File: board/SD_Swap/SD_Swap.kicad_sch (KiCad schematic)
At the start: 45 parts, among them J1 USB_C, Q1 Q_Dual_PNP_PNP_E1B1C2E2B2C1, U1 74LVC2G14, U2 RTS5306E, U3 PCB_SD, U4 93AAxxAT, U5 TS3A27518ERTW, U6 SD_SOCKET, U7 AZ1117-3.3, Y1 12MHz

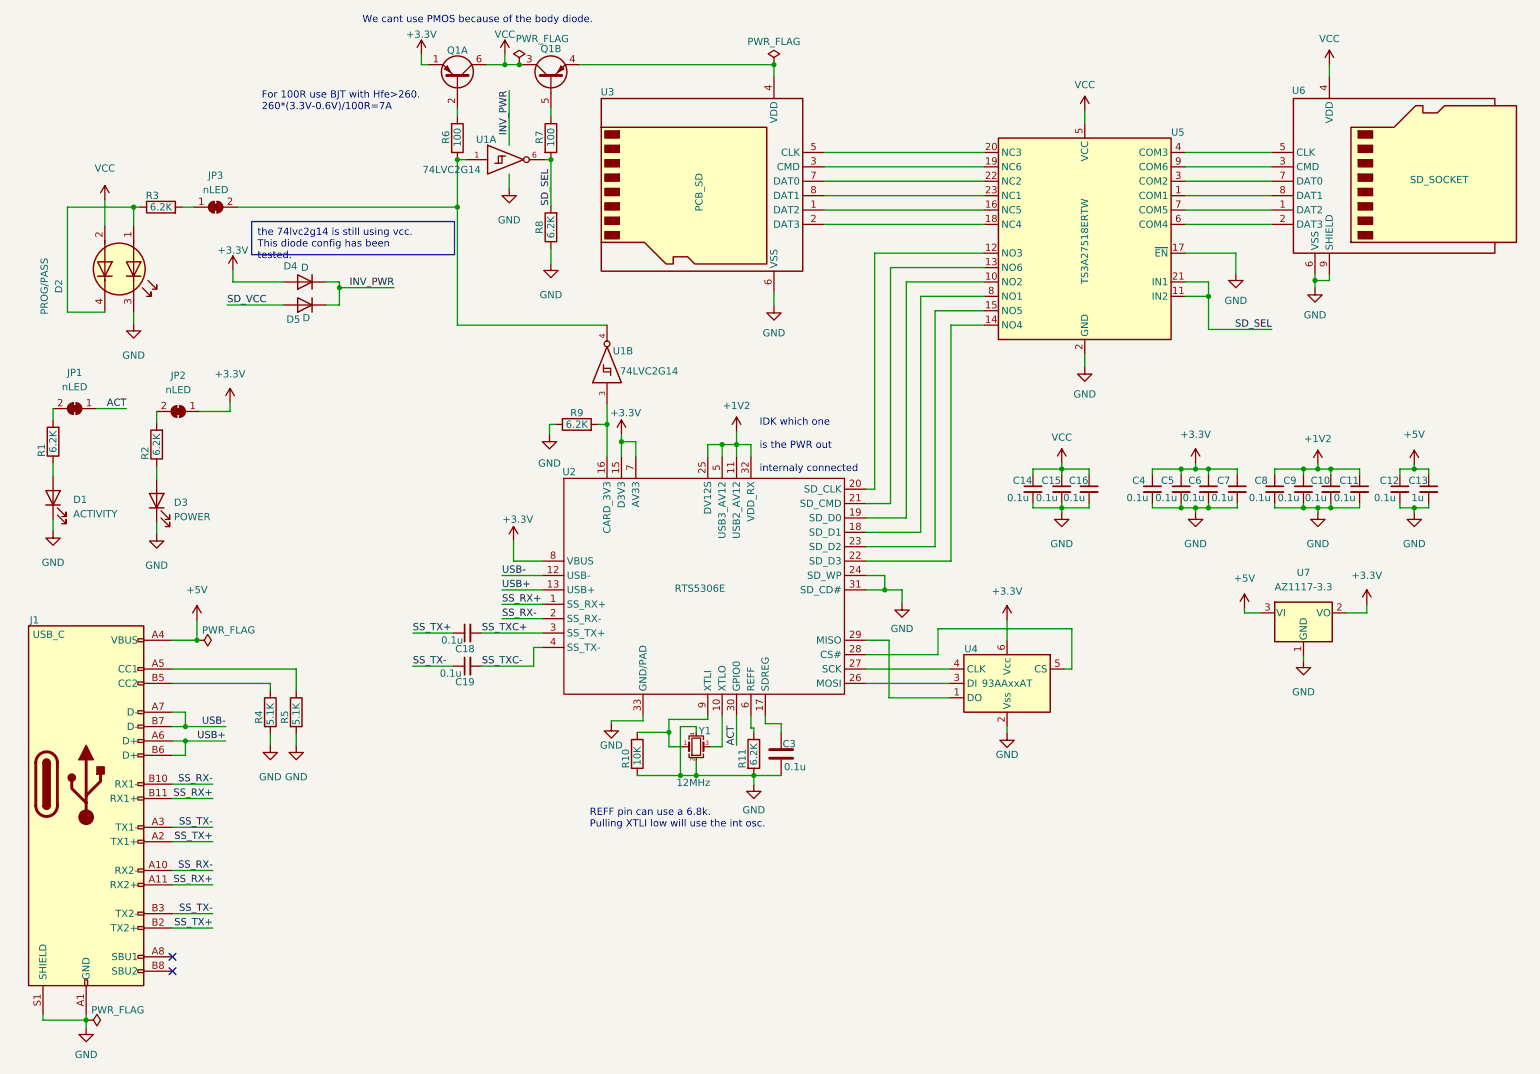
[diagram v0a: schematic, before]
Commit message: update PCB to fix USB3 issues
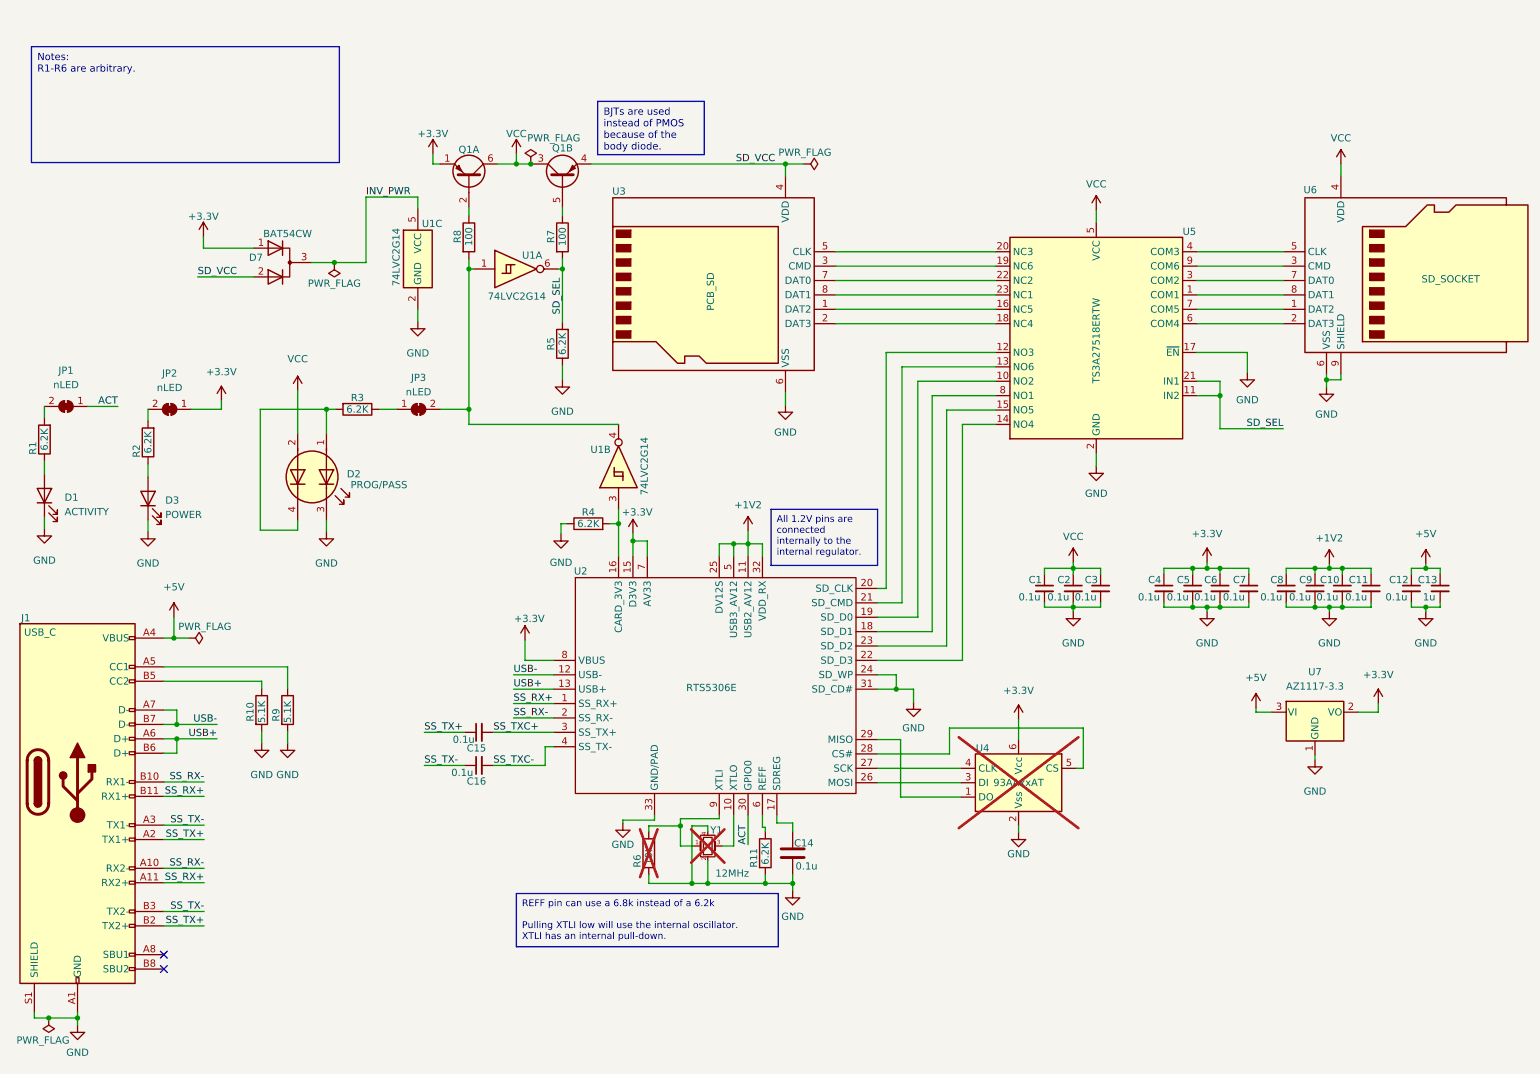
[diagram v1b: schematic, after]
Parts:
- removed D4, D5: D, Diode_SMD:D_0201_0603Metric, symbol Device:D
- added D7: BAT54CW, Package_TO_SOT_SMD:SOT-323_SC-70, symbol Device:D_Dual_CommonCathode_AAK_Parallel
- added unit 3 of U1
- JP1, JP2, JP3, U3: now left out of the parts list
- R6: renamed from R10; now not fitted; now left out of the parts list
- U1: footprint Package_TO_SOT_SMD:SOT-23-6 -> Package_TO_SOT_SMD:SOT-363_SC-70-6; LCSC C12401 -> C3294721
- U4, Y1: now not fitted; now left out of the parts list
- renumbered C14 to C1, C3 to C14, C18 to C15, C19 to C16, C15 to C2, C16 to C3, R4 to R10, R9 to R4, R8 to R5, R6 to R8, R5 to R9
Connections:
- net +3.3V: now also D7.1 (K)
- net GND: now also U1.2 (GND); no longer U1.2 (GND), U1.2 (GND)
- net SD_VCC: now also Q1.4 (E2), U3.4 (VDD), D7.2 (K)
- net VCC: no longer U1.5 (VCC), U1.5 (VCC)
- net at JP3.1 (A): now also R3.1; no longer R3.2
- net at D2.1 (A1), D2.4 (K2): now also R3.2; no longer R3.1
- new net INV_PWR: D7.3 (A), U1.5 (VCC)
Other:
- note removed: "For 100R use BJT with Hfe>260. 260*(3.3V-0.6V)/100R=7A"
- note removed: "IDK which one is the PWR out internaly connected"
- note removed: "REFF pin can use a 6.8k. Pulling XTLI low will use the int osc."
- note removed: "We cant use PMOS because of the body diode."
- title: (none) -> SD SWAP
- moved on the sheet: C1, C10, C11, C12, C13, C14, C15, C16, C2, C3, C4, C5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

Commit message: tmp
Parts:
- J1: footprint Connector_USB:USB_C_Receptacle_Amphenol_12401548E4-2A -> USB-C:USB_C_Receptacle_Amphenol_10137061-00021LF; LCSC C3197851 -> C3197967; Part Number 12401548E4 -> 10137061-00021LF
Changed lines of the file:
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@@
       (effects (font (size 1.27 1.27)))
     )
-    (property "Footprint" "Connector_USB:USB_C_Receptacle_Amphenol_12401548E4-2A" (at 29.972 147.701 0)
+    (property "Footprint" "USB-C:USB_C_Receptacle_Amphenol_10137061-00021LF" (at 29.972 147.701 0)
       (effects (font (size 1.27 1.27)) hide)
     )
-    (property "Datasheet" "https://www.usb.org/sites/default/files/documents/usb_type-c.zip" (at 29.972 147.701 0)
+    (property "Datasheet" "https://www.amphenol-cs.com/media/wysiwyg/files/drawing/10137061.pdf" (at 29.972 147.701 0)
       (effects (font (size 1.27 1.27)) hide)
     )
-    (property "LCSC" "C3197851" (at 26.162 147.701 0)
+    (property "LCSC" "C3197967" (at 26.162 147.701 0)
       (effects (font (size 1.27 1.27)) hide)
     )
-    (property "Part Number" "12401548E4" (at 26.162 147.701 0)
+    (property "Part Number" "10137061-00021LF" (at 26.162 147.701 0)
       (effects (font (size 1.27 1.27)) hide)
     )

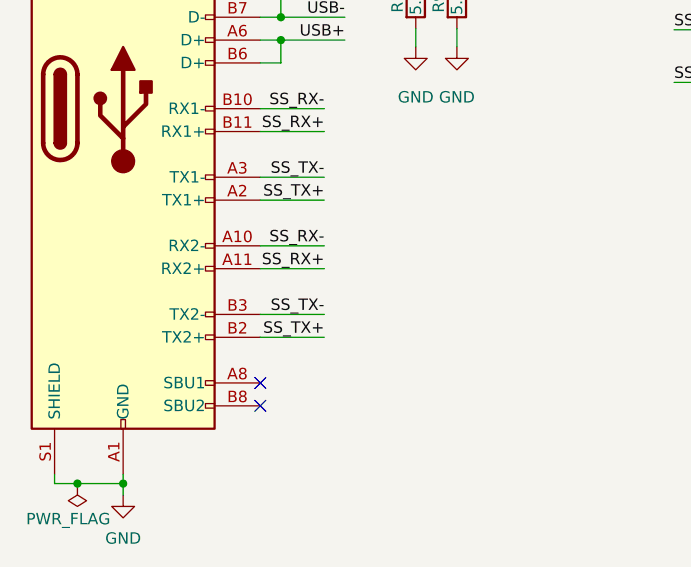
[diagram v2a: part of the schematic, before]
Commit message: I did USB-C wrong in the stupidest way
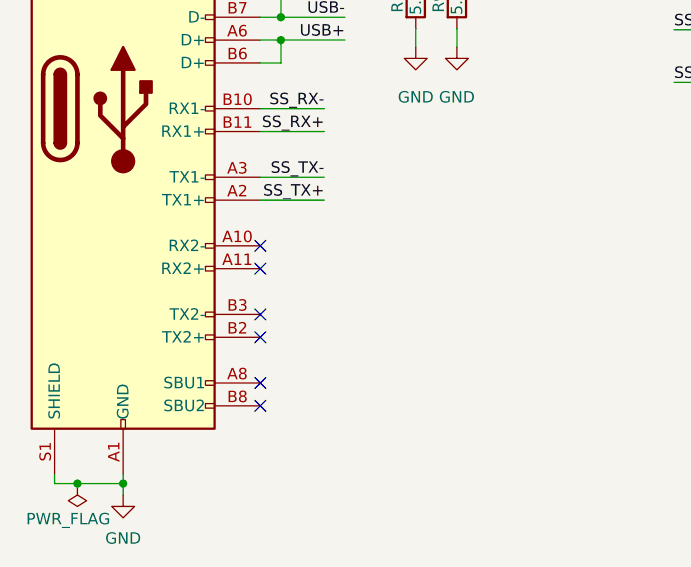
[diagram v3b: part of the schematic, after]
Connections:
- net SS_RX+: no longer J1.A11 (RX2+)
- net SS_RX-: no longer J1.A10 (RX2-)
- net SS_TX+: no longer J1.B2 (TX2+)
- net SS_TX-: no longer J1.B3 (TX2-)
- no-connect marks 2 -> 6
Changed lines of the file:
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@@
   )
   (no_connect (at 41.402 178.181))
+  (no_connect (at 41.402 162.941))
+  (no_connect (at 41.402 170.561))
+  (no_connect (at 41.402 173.101))
+  (no_connect (at 41.402 165.481))
   (no_connect (at 41.402 180.721))
   (wire (pts (xy 132.588 155.448) (xy 132.588 159.004))
@@
     (stroke (width 0) (type default))
   )
-  (wire (pts (xy 48.514 162.941) (xy 41.402 162.941))
-    (stroke (width 0) (type default))
-  )
   (wire (pts (xy 111.506 102.108) (xy 112.522 102.108))
     (stroke (width 0) (type default))
@@
     (stroke (width 0) (type default))
   )
-  (wire (pts (xy 48.514 165.481) (xy 41.402 165.481))
-    (stroke (width 0) (type default))
-  )
   (wire (pts (xy 26.162 188.341) (xy 26.162 189.357))
     (stroke (width 0) (type default))
@@
     (stroke (width 0) (type default))
   )
-  (wire (pts (xy 48.514 173.101) (xy 41.402 173.101))
-    (stroke (width 0) (type default))
-  )
   (wire (pts (xy 223.774 61.722) (xy 239.014 61.722))
     (stroke (width 0) (type default))
@@
   )
   (wire (pts (xy 79.375 81.915) (xy 82.55 81.915))
-    (stroke (width 0) (type default))
-  )
-  (wire (pts (xy 48.514 170.561) (xy 41.402 170.561))
     (stroke (width 0) (type default))
   )
@@
     (effects (font (size 1.27 1.27)) (justify left bottom))
   )
-  (label "SS_RX-" (at 48.514 162.941 180) (fields_autoplaced)
-    (effects (font (size 1.27 1.27)) (justify right bottom))
-  )
   (label "SS_RX-" (at 48.514 147.701 180) (fields_autoplaced)
     (effects (font (size 1.27 1.27)) (justify right bottom))
   )
-  (label "SS_TX-" (at 48.514 170.561 180) (fields_autoplaced)
-    (effects (font (size 1.27 1.27)) (justify right bottom))
-  )
-  (label "SS_TX+" (at 48.514 173.101 180) (fields_autoplaced)
-    (effects (font (size 1.27 1.27)) (justify right bottom))
-  )
   (label "SS_RX+" (at 48.514 150.241 180) (fields_autoplaced)
     (effects (font (size 1.27 1.27)) (justify right bottom))
@@
     (effects (font (size 1.27 1.27)) (justify left bottom))
   )
-  (label "SS_RX+" (at 48.514 165.481 180) (fields_autoplaced)
-    (effects (font (size 1.27 1.27)) (justify right bottom))
-  )
   (label "SD_SEL" (at 239.014 85.344 180) (fields_autoplaced)

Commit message: tmp
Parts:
- D2: symbol Device:LED_Dual_AAKK -> Device:LED_Dual_AKKA
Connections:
- net GND: now also D2.2 (K1); no longer D2.3 (K1)
- net VCC: now also D2.4 (A2); no longer D2.2 (A2)
- net at D2.1 (A1), R3.2: now also D2.3 (K2); no longer D2.4 (K2)
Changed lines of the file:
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@@
   (junction (at 144.526 105.664) (diameter 0) (color 0 0 0 0)
   )
+  (junction (at 95.25 81.915) (diameter 0) (color 0 0 0 0)
+  )
   (junction (at 21.082 189.357) (diameter 0) (color 0 0 0 0)
   )
@@
   (junction (at 223.012 109.982) (diameter 0) (color 0 0 0 0)
   )
-  (junction (at 95.25 81.915) (diameter 0) (color 0 0 0 0)
-  )
   (junction (at 227.838 116.84) (diameter 0) (color 0 0 0 0)
   )
@@
     (stroke (width 0) (type default))
   )
-  (wire (pts (xy 95.25 81.915) (xy 95.25 84.582))
-    (stroke (width 0) (type default))
-  )
   (wire (pts (xy 246.634 76.708) (xy 249.174 76.708))
     (stroke (width 0) (type default))
@@
     (stroke (width 0) (type default))
   )
-  (wire (pts (xy 121.666 84.582) (xy 95.25 84.582))
-    (stroke (width 0) (type default))
-  )
   (wire (pts (xy 26.162 188.341) (xy 26.162 189.357))
     (stroke (width 0) (type default))
@@
     (stroke (width 0) (type default))
   )
+  (wire (pts (xy 95.25 81.915) (xy 121.666 81.915))
+    (stroke (width 0) (type default))
+  )
   (wire (pts (xy 57.277 58.547) (xy 47.371 58.547))
     (stroke (width 0) (type default))
@@
     (stroke (width 0) (type default))
   )
+  (wire (pts (xy 121.666 81.915) (xy 121.666 84.582))
+    (stroke (width 0) (type default))
+  )
   (wire (pts (xy 38.608 91.567) (xy 38.608 93.853))
     (stroke (width 0) (type default))
@@
   )
   (symbol (lib_id "power:GND") (at 111.76 76.708 0) (unit 1)
-    (in_bom yes) (on_board yes) (dnp no) (fields_autoplaced)
+    (in_bom yes) (on_board yes) (dnp no)
     (property "Reference" "#PWR0133" (at 111.76 83.058 0)
       (effects (font (size 1.27 1.27)) hide)
     )
-    (property "Value" "GND" (at 111.76 82.296 0)
+    (property "Value" "GND" (at 111.76 80.391 0)
       (effects (font (size 1.27 1.27)))
     )
@@
     )
   )
-  (symbol (lib_id "Device:LED_Dual_AAKK") (at 67.564 93.853 270) (unit 1)
+  (symbol (lib_id "Device:LED_Dual_AKKA") (at 67.564 93.853 270) (unit 1)
     (in_bom yes) (on_board yes) (dnp no)
     (property "Reference" "D2" (at 74.93 93.345 90)
